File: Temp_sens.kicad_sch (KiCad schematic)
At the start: 16 parts, among them J301 PT_1000, Q301 IRLML5103, U301 ADA4807-1

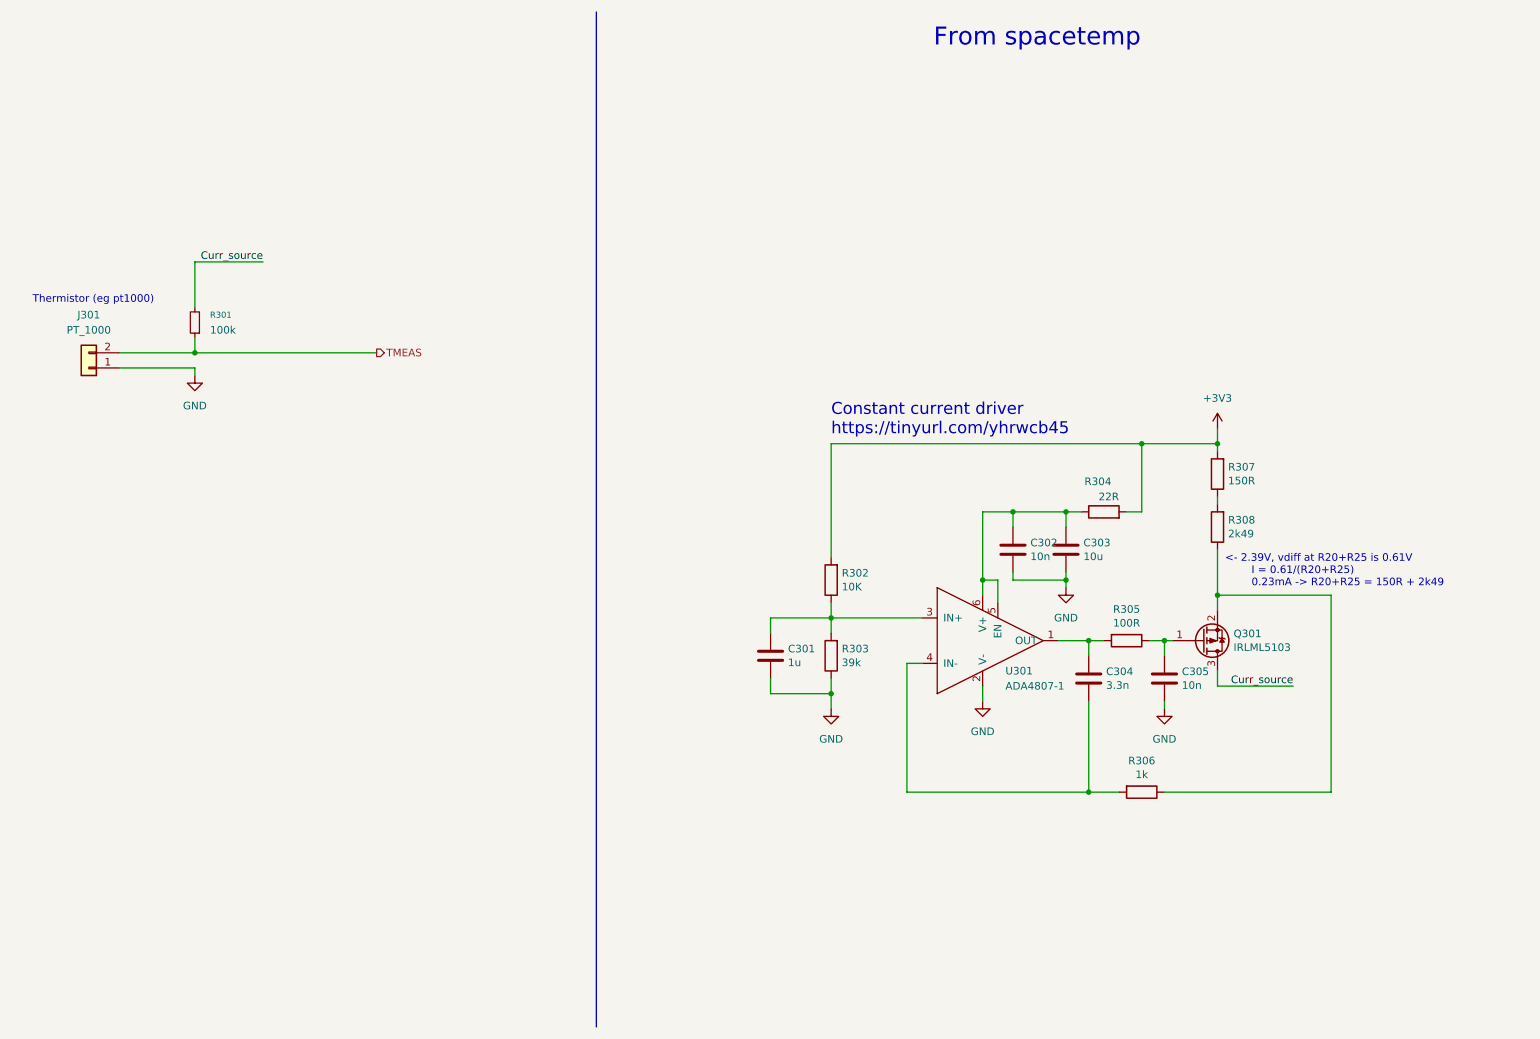
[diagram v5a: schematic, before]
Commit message: added missing heater connectors
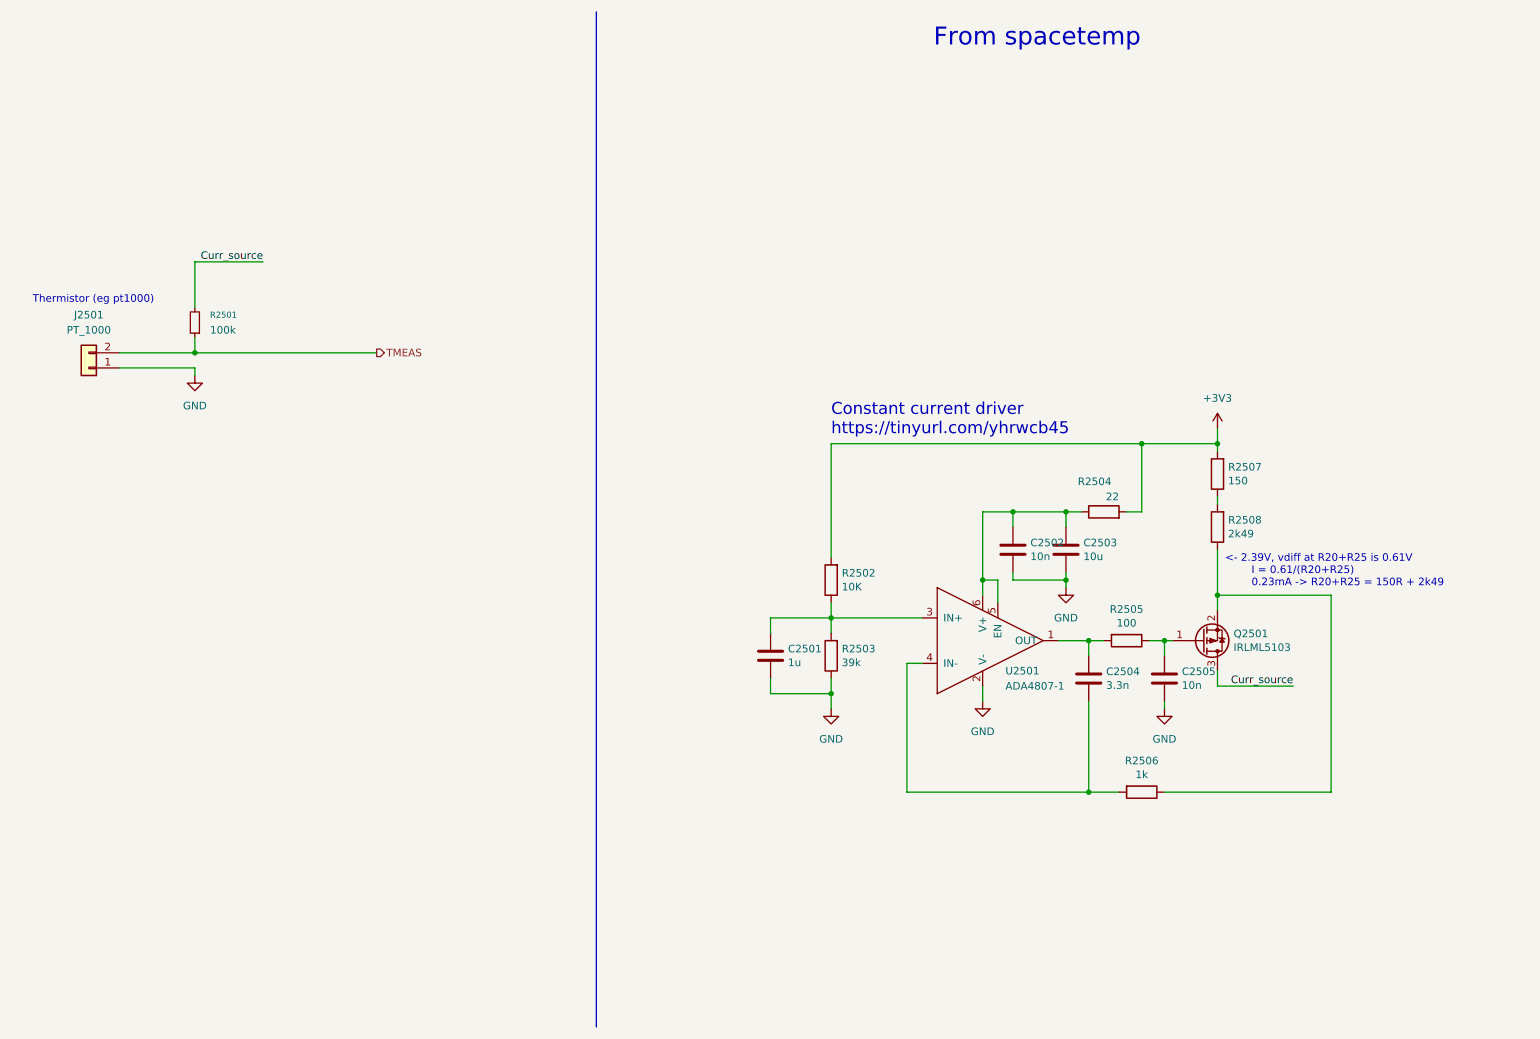
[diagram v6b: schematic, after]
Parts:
- R2504: renamed from R304; value 22R -> 22
- R2505: renamed from R305; value 100R -> 100
- R2507: renamed from R307; value 150R -> 150
- renumbered C301 to C2501, C302 to C2502, C303 to C2503, C304 to C2504, C305 to C2505, J301 to J2501, Q301 to Q2501, R301 to R2501, R302 to R2502, R303 to R2503, R306 to R2506, R308 to R2508, U301 to U2501
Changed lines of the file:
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@@
 		(on_board yes)
 		(dnp no)
-		(property "Reference" "U301"
+		(property "Reference" "U2501"
 			(at 199.39 128.27 0)
 			(effects
@@
 		(on_board yes)
 		(dnp no)
-		(property "Reference" "C302"
+		(property "Reference" "C2502"
 			(at 203.581 106.7816 0)
 			(effects
@@
 		(on_board yes)
 		(dnp no)
-		(property "Reference" "C303"
+		(property "Reference" "C2503"
 			(at 212.471 106.7816 0)
 			(effects
@@
 		(on_board yes)
 		(dnp no)
-		(property "Reference" "R304"
+		(property "Reference" "R2504"
 			(at 217.17 96.52 90)
 			(effects
@@
 			)
 		)
-		(property "Value" "22R"
+		(property "Value" "22"
 			(at 218.44 99.06 90)
 			(effects
@@
 		(on_board yes)
 		(dnp no)
-		(property "Reference" "Q301"
+		(property "Reference" "Q2501"
 			(at 237.6424 122.0216 0)
 			(effects
@@
 		(on_board yes)
 		(dnp no)
-		(property "Reference" "R307"
+		(property "Reference" "R2507"
 			(at 236.728 94.0816 0)
 			(effects
@@
 			)
 		)
-		(property "Value" "150R"
+		(property "Value" "150"
 			(at 236.728 96.393 0)
 			(effects
@@
 		(on_board yes)
 		(dnp no)
-		(property "Reference" "R305"
+		(property "Reference" "R2505"
 			(at 219.71 117.9322 90)
 			(effects
@@
 			)
 		)
-		(property "Value" "100R"
+		(property "Value" "100"
 			(at 219.71 120.2436 90)
 			(effects
@@
 		(on_board yes)
 		(dnp no)
-		(property "Reference" "R302"
+		(property "Reference" "R2502"
 			(at 171.958 111.8616 0)
 			(effects
@@
 		(on_board yes)
 		(dnp no)
-		(property "Reference" "R303"
+		(property "Reference" "R2503"
 			(at 171.958 124.5616 0)
 			(effects
@@
 		(on_board yes)
 		(dnp no)
-		(property "Reference" "C301"
+		(property "Reference" "C2501"
 			(at 162.941 124.5616 0)
 			(effects
@@
 		(on_board yes)
 		(dnp no)
-		(property "Reference" "R308"
+		(property "Reference" "R2508"
 			(at 236.728 102.9716 0)
 			(effects
@@
 		(dnp no)
 		(fields_autoplaced yes)
-		(property "Reference" "R301"
+		(property "Reference" "R2501"
 			(at 66.04 68.5799 0)
 			(effects
@@
 		(on_board yes)
 		(dnp no)
-		(property "Reference" "R306"
+		(property "Reference" "R2506"
 			(at 222.25 143.3322 90)
 			(effects
@@
 		(on_board yes)
 		(dnp no)
-		(property "Reference" "C304"
+		(property "Reference" "C2504"
 			(at 216.281 128.3716 0)
 			(effects
@@
 		(dnp no)
 		(fields_autoplaced yes)
-		(property "Reference" "#PWR0304"
+		(property "Reference" "#PWR02504"
 			(at 209.55 120.65 0)
 			(effects
@@
 		(dnp no)
 		(fields_autoplaced yes)
-		(property "Reference" "#PWR0303"
+		(property "Reference" "#PWR02503"
 			(at 195.58 139.7 0)
 			(effects
@@
 		(dnp no)
 		(fields_autoplaced yes)
-		(property "Reference" "#PWR0302"
+		(property "Reference" "#PWR02502"
 			(at 170.18 140.97 0)
 			(effects
@@
 		(dnp no)
 		(fields_autoplaced yes)
-		(property "Reference" "#PWR0301"
+		(property "Reference" "#PWR02501"
 			(at 63.5 85.09 0)
 			(effects
@@
 		(dnp no)
 		(fields_autoplaced yes)
-		(property "Reference" "J301"
+		(property "Reference" "J2501"
 			(at 45.72 68.58 0)
 			(effects
@@
 		(dnp no)
 		(fields_autoplaced yes)
-		(property "Reference" "#PWR0305"
+		(property "Reference" "#PWR02505"
 			(at 226.06 140.97 0)
 			(effects
@@
 		(on_board yes)
 		(dnp no)
-		(property "Reference" "C305"
+		(property "Reference" "C2505"
 			(at 228.981 128.3716 0)
 			(effects
@@
 		(dnp no)
 		(fields_autoplaced yes)
-		(property "Reference" "#PWR0306"
+		(property "Reference" "#PWR02506"
 			(at 234.95 91.44 0)
 			(effects

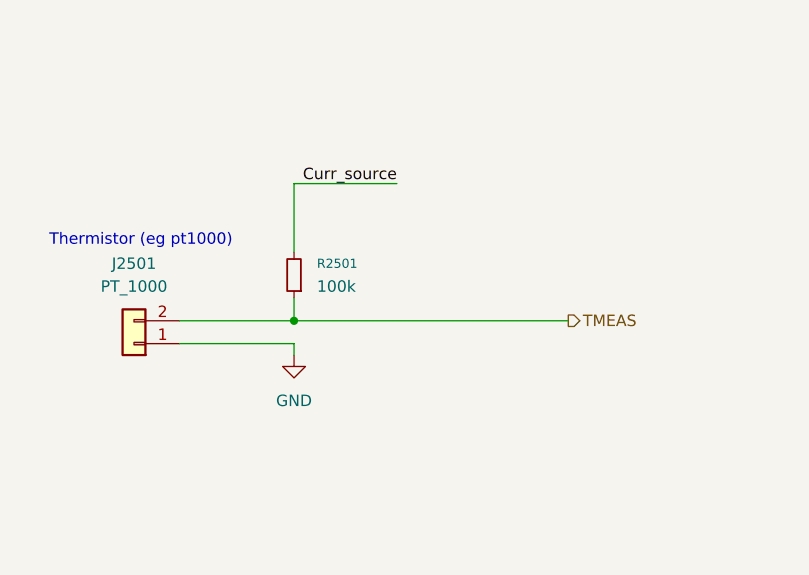
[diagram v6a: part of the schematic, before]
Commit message: replaced individual CC sourses for SOL with a single one
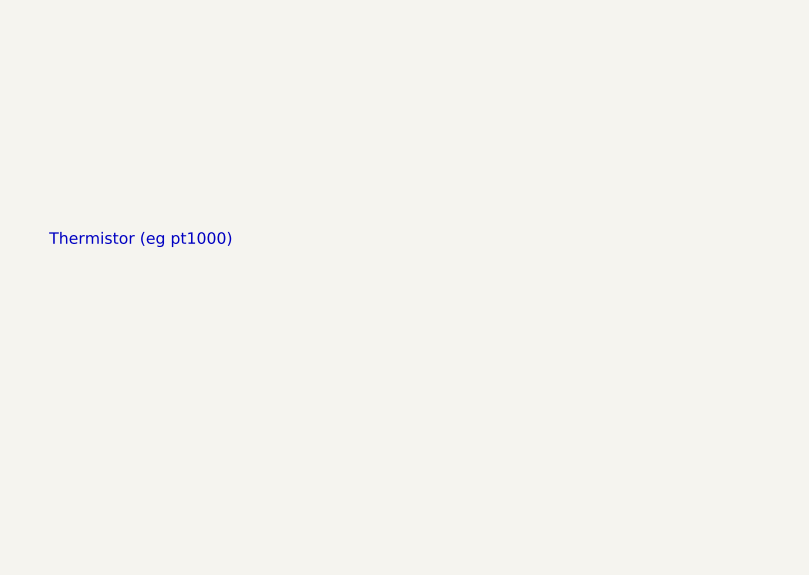
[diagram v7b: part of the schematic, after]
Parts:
- removed J2501: PT_1000, Connector_PinSocket_2.54mm:PinSocket_1x02_P2.54mm_Vertical, symbol Connector_Generic:Conn_01x02
- removed R2501: 100k, Resistor_SMD:R_0603_1608Metric_Pad0.98x0.95mm_HandSolder, symbol Device:R_Small
